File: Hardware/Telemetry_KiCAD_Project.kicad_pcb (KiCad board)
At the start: 4 copper layers, 80 x 93.3 mm, 68 parts, among them J1 TX SPI Debug, J2 RX SPI Debug, J3 50Ω SMA Connector, J4 10118192-0001LF, J5 DB37_Male_MountingHoles, U1 STM32L562VET, U2 Si4463, U3 Si4463, U4 ADL5521, U5 RSD-897.500-942.500-1612-TR, U6 LM317T, U7 USBLC6-2SC6, Y1 32MHz, Y2 32MHz, Y3 32MHz

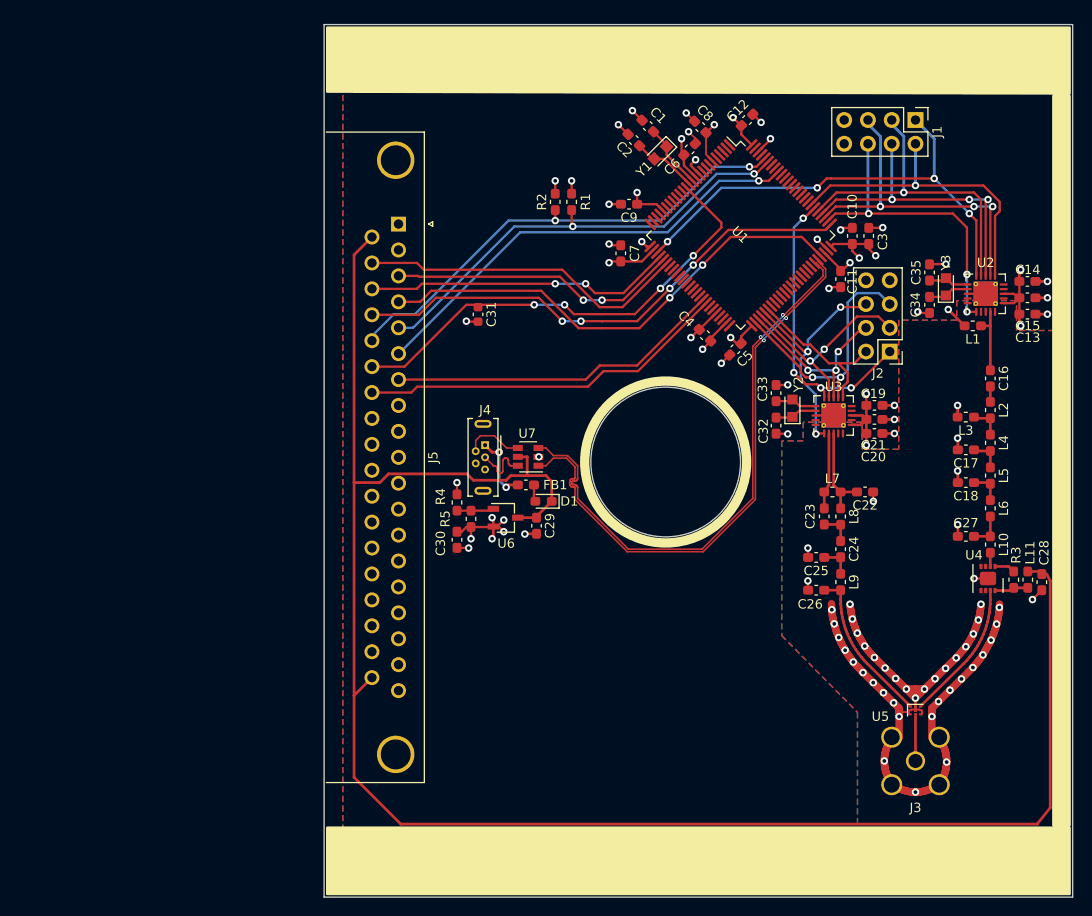
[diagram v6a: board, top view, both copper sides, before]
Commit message: Major Redesign
 - Copper ground pours on F and B.
 - Improved isolation between data lines
 - Expanded via fences around RF section.
 - GND plane isolation peninsulas for crystals.
 - Simplified I2C, SPI, and USB lines for reduced interference.
 - Added 3D models for all components.
 - Adjusted positions of RF components for improved impedance matching.
 - RF components to 0402 package from 0603 for improved impedance matching.
 - Traces for RF section have rounded corners to help improve impedance matching and reduce interference.
 - Moved silkscreen labels to outside via fence for improved legibility.
 - Improved trace thicknesses for power delivery.
 - Updated libraries to include those found in other RDT modules.
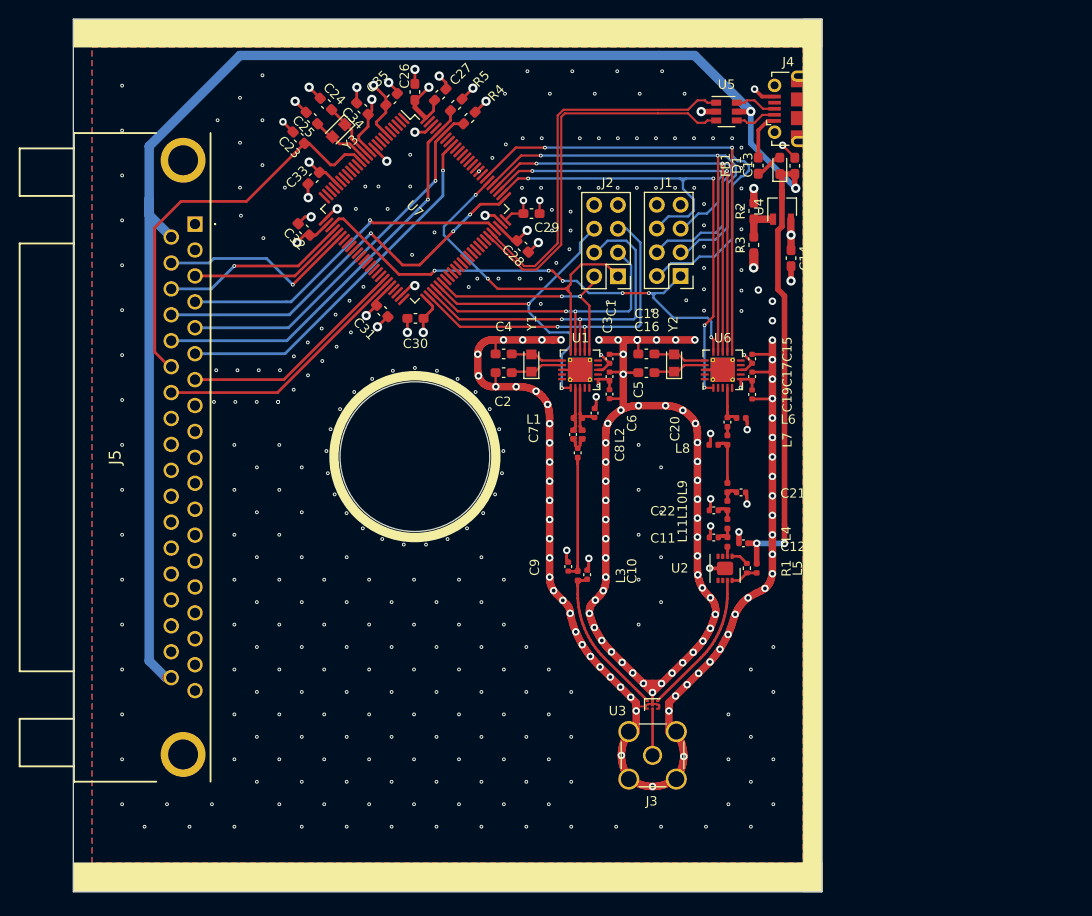
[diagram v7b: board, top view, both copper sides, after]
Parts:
- C1: value 30pF -> 100pF; footprint Capacitor_SMD:C_0603_1608Metric_Pad1.08x0.95mm_HandSolder -> Capacitor_SMD:C_0402_1005Metric
- C10, C9: value 100nF -> 4.3pF; footprint Capacitor_SMD:C_0603_1608Metric_Pad1.08x0.95mm_HandSolder -> Capacitor_SMD:C_0402_1005Metric
- C11: value 100nF -> 2.4pF; footprint Capacitor_SMD:C_0603_1608Metric_Pad1.08x0.95mm_HandSolder -> Capacitor_SMD:C_0402_1005Metric
- C12: footprint Capacitor_SMD:C_0603_1608Metric_Pad1.08x0.95mm_HandSolder -> Capacitor_SMD:C_0402_1005Metric
- C13: value 100pF -> 0.1uF
- C14: value 100pF -> 1uF
- C15, C3: value 1uF -> 100pF; footprint Capacitor_SMD:C_0603_1608Metric_Pad1.08x0.95mm_HandSolder -> Capacitor_SMD:C_0402_1005Metric
- C16: value 4.7pF -> 30pF
- C17: value 3.3pF -> 100pF; footprint Capacitor_SMD:C_0603_1608Metric_Pad1.08x0.95mm_HandSolder -> Capacitor_SMD:C_0402_1005Metric
- C18: value 3.3pF -> 30pF
- C19: value 100pF -> 1uF; footprint Capacitor_SMD:C_0603_1608Metric_Pad1.08x0.95mm_HandSolder -> Capacitor_SMD:C_0402_1005Metric
- C20: value 100pF -> 4.7pF; footprint Capacitor_SMD:C_0603_1608Metric_Pad1.08x0.95mm_HandSolder -> Capacitor_SMD:C_0402_1005Metric
- C21: value 1uF -> 3.3pF; footprint Capacitor_SMD:C_0603_1608Metric_Pad1.08x0.95mm_HandSolder -> Capacitor_SMD:C_0402_1005Metric
- C22: value 3pF -> 3.3pF; footprint Capacitor_SMD:C_0603_1608Metric_Pad1.08x0.95mm_HandSolder -> Capacitor_SMD:C_0402_1005Metric
- C23: value 1pF -> 100nF
- C24: value DC_Blocking -> 30pF
- C25: value 4.3pF -> 30pF
- C26: value 4.3pF -> 1uF
- C27: value 2.4pF -> 100nF
- C29: value 0.1uF -> 100nF
- C30: value 1uF -> 100nF
- C31: footprint Capacitor_SMD:C_0603_1608Metric -> Capacitor_SMD:C_0603_1608Metric_Pad1.08x0.95mm_HandSolder
- C32, C33, C34, C35: value 30pF -> 100nF
- C4: value 100nF -> 30pF
- C5: value 100nF -> 1uF; footprint Capacitor_SMD:C_0603_1608Metric_Pad1.08x0.95mm_HandSolder -> Capacitor_SMD:C_0402_1005Metric
- C6: value 100nF -> 3pF; footprint Capacitor_SMD:C_0603_1608Metric_Pad1.08x0.95mm_HandSolder -> Capacitor_SMD:C_0402_1005Metric
- C7: value 100nF -> 1pF; footprint Capacitor_SMD:C_0603_1608Metric_Pad1.08x0.95mm_HandSolder -> Capacitor_SMD:C_0402_1005Metric
- C8: value 100nF -> DC_Blocking; footprint Capacitor_SMD:C_0603_1608Metric_Pad1.08x0.95mm_HandSolder -> Capacitor_SMD:C_0402_1005Metric
- J3: value 50Ω SMA Connector -> Amphenol 132134 SMA Connector
- J4: footprint Connector_USB:USB_Micro-B_Wuerth_614105150721_Vertical -> Connector_USB:USB_Micro-B_Molex-105017-0001
- J5: footprint Connector_Dsub:DSUB-37_Male_Horizontal_P2.77x2.84mm_EdgePinOffset4.94mm_Housed_MountingHolesOffset7.48mm -> RDT_Custom_Footprints:L717SDC37P1ACH4F
- L1: value 100nH -> 18nH; footprint Inductor_SMD:L_0603_1608Metric_Pad1.05x0.95mm_HandSolder -> Inductor_SMD:L_0402_1005Metric
- L10: value 8.2nH -> 22nH; footprint Inductor_SMD:L_0603_1608Metric_Pad1.05x0.95mm_HandSolder -> Inductor_SMD:L_0402_1005Metric
- L11: value 3.4nH -> 11nH; footprint Inductor_SMD:L_0603_1608Metric_Pad1.05x0.95mm_HandSolder -> Inductor_SMD:L_0402_1005Metric
- L2: value 3.3nH -> 22nH; footprint Inductor_SMD:L_0603_1608Metric_Pad1.05x0.95mm_HandSolder -> Inductor_SMD:L_0402_1005Metric
- L3: value 6.2nH -> 8.2nH; footprint Inductor_SMD:L_0603_1608Metric_Pad1.05x0.95mm_HandSolder -> Inductor_SMD:L_0402_1005Metric
- L4: value 11nH -> 8.2nH; footprint Inductor_SMD:L_0603_1608Metric_Pad1.05x0.95mm_HandSolder -> Inductor_SMD:L_0402_1005Metric
- L5: value 22nH -> 3.4nH; footprint Inductor_SMD:L_0603_1608Metric_Pad1.05x0.95mm_HandSolder -> Inductor_SMD:L_0402_1005Metric
- L6: value 11nH -> 100nH; footprint Inductor_SMD:L_0603_1608Metric_Pad1.05x0.95mm_HandSolder -> Inductor_SMD:L_0402_1005Metric
- L7: value 18nH -> 3.3nH; footprint Inductor_SMD:L_0603_1608Metric_Pad1.05x0.95mm_HandSolder -> Inductor_SMD:L_0402_1005Metric
- L8: value 22nH -> 6.2nH; footprint Inductor_SMD:L_0603_1608Metric_Pad1.05x0.95mm_HandSolder -> Inductor_SMD:L_0402_1005Metric
- L9: value 8.2nH -> 11nH; footprint Inductor_SMD:L_0603_1608Metric_Pad1.05x0.95mm_HandSolder -> Inductor_SMD:L_0402_1005Metric
- R1: value 4.7k -> 1.3k; footprint Resistor_SMD:R_0603_1608Metric_Pad1.05x0.95mm_HandSolder -> Resistor_SMD:R_0402_1005Metric
- R2: value 4.7k -> 390Ω
- R3: value 1.3k -> 240Ω
- R4: value 390Ω -> 4.7k
- R5: value 240Ω -> 4.7k
- U1: value STM32L562VET -> Si4463; footprint Package_QFP:LQFP-100_14x14mm_P0.5mm -> Package_DFN_QFN:QFN-20-1EP_4x4mm_P0.5mm_EP2.6x2.6mm_ThermalVias
- U2: value Si4463 -> ADL5521; footprint Package_DFN_QFN:QFN-20-1EP_4x4mm_P0.5mm_EP2.6x2.6mm_ThermalVias -> Package_CSP:LFCSP-8-1EP_3x3mm_P0.5mm_EP1.45x1.74mm
- U3: value Si4463 -> RSD-897.500-942.500-1612-TR; footprint Package_DFN_QFN:QFN-20-1EP_4x4mm_P0.5mm_EP2.6x2.6mm_ThermalVias -> RDT_Custom_Footprints:RSD-897.500-942.500-1612-TR
- U4: value ADL5521 -> LM317T; footprint Package_CSP:LFCSP-8-1EP_3x3mm_P0.5mm_EP1.45x1.74mm -> Package_TO_SOT_SMD:TSOT-23
- U5: value RSD-897.500-942.500-1612-TR -> USBLC6-2SC6; footprint RDT_Custom_Footprints:RSD-897.500-942.500-1612-TR -> Package_TO_SOT_SMD:SOT-23-6
- U6: value LM317T -> Si4463; footprint Package_TO_SOT_SMD:TSOT-23 -> Package_DFN_QFN:QFN-20-1EP_4x4mm_P0.5mm_EP2.6x2.6mm_ThermalVias
- U7: value USBLC6-2SC6 -> STM32L562VET6Q; footprint Package_TO_SOT_SMD:SOT-23-6 -> Package_QFP:LQFP-100_14x14mm_P0.5mm
- moved C27 73.4 mm to (119.2, 59.8), turned to 45 degrees
- moved C24 72.7 mm to (107.0, 60.8), turned to 135 degrees
- moved C25 71.5 mm to (105.5, 62.3), turned to 135 degrees
- moved C23 69.2 mm to (104.1, 64.4), turned to 135 degrees
- moved C26 68.4 mm to (116.5, 59.5), turned to 90 degrees
- moved Y3 67.0 mm to (108.4, 63.6), turned to 225 degrees
- moved U5 66.3 mm to (149.8, 61.6)
- moved C28 66.1 mm to (128.0, 76.0), turned to 315 degrees
- moved C34 64.1 mm to (110.9, 61.3), turned to 135 degrees
- moved C35 60.4 mm to (114.0, 60.3), turned to 45 degrees
- moved C32 54.6 mm to (104.6, 74.2), turned to 135 degrees
- moved C33 54.5 mm to (105.7, 68.7), turned to 225 degrees
- moved J4 48.4 mm to (156.4, 61.3), turned to 90 degrees
- moved C10 46.0 mm to (134.9, 111.1)
- moved U4 45.4 mm to (155.7, 71.8), turned to 90 degrees
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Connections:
- C1 pad 1: Net-(C1-Pad1) -> GND
- C1 pad 2: GND -> +3V3
- C10 pad 1: +3V3 -> /RX_Si4463/RF_Out
- C11 pad 1: +3V3 -> GND
- C11 pad 2: GND -> /ADL_Amplifier/RF_In
- C12 pad 1: +3V3 -> GND
- C12 pad 2: GND -> +5V
- C13 pad 1: GND -> +5V
- C13 pad 2: +3V3 -> GND
- C14 pad 1: GND -> +3V3
- C14 pad 2: +3V3 -> GND
- C16 pad 2: Net-(C16-Pad2) -> GND
- C17 pad 1: Net-(C17-Pad1) -> GND
- C17 pad 2: GND -> +3V3
- C20 pad 1: GND -> Net-(C20-Pad1)
- C20 pad 2: +3V3 -> Net-(C20-Pad2)
- C21 pad 1: GND -> Net-(C21-Pad1)
- C21 pad 2: +3V3 -> GND
- C22 pad 1: GND -> Net-(C22-Pad1)
- C22 pad 2: Net-(C22-Pad2) -> GND
- C23 pad 1: Net-(C23-Pad1) -> /37 Pin DSUB/NRST
- C23 pad 2: Net-(C23-Pad2) -> GND
- C24 pad 1: Net-(C23-Pad2) -> Net-(C24-Pad1)
- C24 pad 2: Net-(C24-Pad2) -> GND
- C25 pad 1: Net-(C24-Pad2) -> Net-(C25-Pad1)
- C26 pad 1: /RX_Si4463/RF_Out -> +3V3
- C27 pad 1: GND -> +3V3
- C27 pad 2: /ADL_Amplifier/RF_In -> GND
- C28 pad 1: GND -> +3V3
- C28 pad 2: +5V -> GND
- C29 pad 1: +5V -> +3V3
- C3 pad 1: +3V3 -> GND
- C3 pad 2: GND -> +3V3
- C31 pad 1: /37 Pin DSUB/NRST -> +3V3
- C32 pad 1: Net-(C32-Pad1) -> +3V3
- C33 pad 1: Net-(C33-Pad1) -> +3V3
- C34 pad 1: Net-(C34-Pad1) -> +3V3
- C35 pad 1: Net-(C35-Pad1) -> +3V3
- C4 pad 1: +3V3 -> Net-(C4-Pad1)
- C5 pad 1: +3V3 -> GND
- C5 pad 2: GND -> +3V3
- C6 pad 1: +3V3 -> GND
- C6 pad 2: GND -> Net-(C6-Pad2)
- C7 pad 1: +3V3 -> Net-(C7-Pad1)
- C7 pad 2: GND -> Net-(C7-Pad2)
- C8 pad 1: +3V3 -> Net-(C7-Pad2)
- C8 pad 2: GND -> Net-(C8-Pad2)
- C9 pad 1: +3V3 -> Net-(C8-Pad2)
- L1 pad 1: Net-(C16-Pad1) -> Net-(C7-Pad1)
- L1 pad 2: +3V3 -> Net-(C6-Pad2)
- L10 pad 1: /ADL_Amplifier/RF_In -> Net-(C21-Pad1)
- L10 pad 2: Net-(L10-Pad2) -> Net-(C22-Pad1)
- L11 pad 1: Net-(L11-Pad1) -> Net-(C22-Pad1)
- L11 pad 2: +5V -> /ADL_Amplifier/RF_In
- L2 pad 1: Net-(C16-Pad2) -> Net-(C6-Pad2)
- L2 pad 2: Net-(L2-Pad2) -> Net-(C7-Pad2)
- L3 pad 1: Net-(L2-Pad2) -> Net-(C8-Pad2)
- L3 pad 2: GND -> /RX_Si4463/RF_Out
- L4 pad 1: Net-(L2-Pad2) -> /ADL_Amplifier/RF_In
- L4 pad 2: Net-(C17-Pad1) -> Net-(L4-Pad2)
- L5 pad 1: Net-(C17-Pad1) -> Net-(L5-Pad1)
- L5 pad 2: Net-(C18-Pad1) -> +5V
- L6 pad 1: Net-(C18-Pad1) -> Net-(C20-Pad1)
- L6 pad 2: /ADL_Amplifier/RF_In -> +3V3
- L7 pad 1: Net-(C23-Pad1) -> Net-(C20-Pad2)
- L7 pad 2: Net-(C22-Pad2) -> Net-(L7-Pad2)
- L8 pad 1: Net-(C22-Pad2) -> Net-(L7-Pad2)
- L8 pad 2: Net-(C23-Pad2) -> GND
- L9 pad 1: Net-(C24-Pad2) -> Net-(L7-Pad2)
- L9 pad 2: /RX_Si4463/RF_Out -> Net-(C21-Pad1)
- R1 pad 1: /37 Pin DSUB/Alert_scl -> Net-(L5-Pad1)
- R1 pad 2: +3V3 -> Net-(R1-Pad2)
- R2 pad 1: /37 Pin DSUB/Alert_sda -> Net-(R2-Pad1)
- R2 pad 2: +3V3 -> GND
- R3 pad 1: Net-(L11-Pad1) -> +3V3
- R3 pad 2: Net-(R3-Pad2) -> Net-(R2-Pad1)
- R4 pad 1: Net-(R4-Pad1) -> /37 Pin DSUB/Alert_scl
- R4 pad 2: GND -> +3V3
- R5 pad 1: +3V3 -> /37 Pin DSUB/Alert_sda
- R5 pad 2: Net-(R4-Pad1) -> +3V3
- U1 pad 1: Net-(U1-Pad1) -> /RX_RST
- U1 pad 10: GND -> Net-(U1-Pad10)
- U1 pad 11: +3V3 -> /~RX_IRQ
- U1 pad 12: Net-(C1-Pad1) -> /RX_SCL
- U1 pad 13: Net-(C2-Pad1) -> /RX_SDO
- U1 pad 14: /37 Pin DSUB/NRST -> /RX_SDI
- U1 pad 15: Net-(U1-Pad15) -> /~RX_SEL
- U1 pad 16: Net-(U1-Pad16) -> Net-(C4-Pad1)
- U1 pad 17: Net-(U1-Pad17) -> Net-(C2-Pad1)
- U1 pad 18: Net-(U1-Pad18) -> GND
- U1 pad 2: Net-(U1-Pad2) -> Net-(C7-Pad1)
- U1 pad 21: +3V3 -> GND
- U1 pad 3: Net-(U1-Pad3) -> Net-(C6-Pad2)
- U1 pad 8: Net-(U1-Pad8) -> +3V3
- U2 pad 1: /TX_RST -> Net-(R1-Pad2)
- U2 pad 2: Net-(U2-Pad2) -> Net-(L4-Pad2)
- U2 pad 3: Net-(U2-Pad3) -> (no net)
- U2 pad 4: Net-(C16-Pad1) -> (no net)
- U2 pad 5: Net-(U2-Pad5) -> (no net)
- U2 pad 6: +3V3 -> (no net)
- U2 pad 7: Net-(U2-Pad7) -> /ADL_Amplifier/RF_Out
- U2 pad 8: +3V3 -> Net-(L5-Pad1)
- U2 pad 9: Net-(U2-Pad9) -> GND
- U3 pad 1: /RX_RST -> /RX_Si4463/RF_Out
- U3 pad 2: Net-(C23-Pad1) -> GND
- U3 pad 3: Net-(C22-Pad2) -> /ADL_Amplifier/RF_Out
- U3 pad 4: Net-(U3-Pad4) -> GND
- U3 pad 5: Net-(U3-Pad5) -> GND
- U3 pad 6: +3V3 -> /RSD_Duplexer/Antenna
- U3 pad 7: Net-(U3-Pad7) -> GND
- U3 pad 8: +3V3 -> GND
- U4 pad 1: Net-(R3-Pad2) -> Net-(R2-Pad1)
- U4 pad 2: Net-(L10-Pad2) -> +3V3
- U4 pad 3: (no net) -> +5V
- U5 pad 1: /RX_Si4463/RF_Out -> /USB Connector and ESD/D+
- U5 pad 3: /ADL_Amplifier/RF_Out -> /USB Connector and ESD/D-
- U5 pad 4: GND -> /USB Connector and ESD/USB_CONN_D-
- U5 pad 5: GND -> +5V
- U5 pad 6: /RSD_Duplexer/Antenna -> /USB Connector and ESD/USB_CONN_D+
- U6 pad 1: Net-(R4-Pad1) -> /TX_RST
- U6 pad 2: +3V3 -> Net-(U6-Pad2)
- U6 pad 3: +5V -> Net-(U6-Pad3)
- U7 pad 1: /USB Connector and ESD/D+ -> Net-(U7-Pad1)
- U7 pad 2: GND -> Net-(U7-Pad2)
- U7 pad 3: /USB Connector and ESD/D- -> Net-(U7-Pad3)
- U7 pad 4: /USB Connector and ESD/USB_CONN_D- -> Net-(U7-Pad4)
- U7 pad 5: +5V -> Net-(U7-Pad5)
- U7 pad 6: /USB Connector and ESD/USB_CONN_D+ -> +3V3
- Y1 pad 1: Net-(C1-Pad1) -> Net-(C2-Pad1)
- Y1 pad 2: Net-(C2-Pad1) -> Net-(C4-Pad1)
- Y2 pad 1: Net-(C32-Pad1) -> Net-(C16-Pad1)
- Y2 pad 2: Net-(C33-Pad1) -> Net-(C18-Pad1)
- Y3 pad 1: Net-(C34-Pad1) -> Net-(C24-Pad1)
- Y3 pad 2: Net-(C35-Pad1) -> Net-(C25-Pad1)
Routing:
- net GND: track 146.9 -> 308.4 mm, vias 79 -> 404
- net /~TX_IRQ: track 34.3 -> 71.0 mm, vias 1 -> 2
- net /TX_SDO: track 32.7 -> 61.5 mm, vias 3 -> 2
- net /TX_SDI: track 35.0 -> 61.8 mm, vias 1 -> 2
- net /TX_RST: track 33.3 -> 56.3 mm, vias 3 -> 4
- net /USB Connector and ESD/D+: track 62.1 -> 40.8 mm, vias 2 -> 0
- net /USB Connector and ESD/D-: track 61.5 -> 41.1 mm, vias 2 -> 0
- net /RX_SDO: track 19.8 -> 39.0 mm, vias 3 -> 2
- net /TX_SCL: track 35.8 -> 53.6 mm, vias 3 -> 2
- net /MCU_L562VE/DEBUG_SWDIO: track 52.2 -> 36.3 mm, vias 2 -> 1
- net Net-(C8-Pad2): track 0.00 -> 14.6 mm
- net /MCU_L562VE/SPI1_MISO: track 31.2 -> 17.1 mm, vias 2 -> 0
- net /MCU_L562VE/SPI1_MOSI: track 35.4 -> 21.6 mm, vias 0 -> 1
- net /MCU_L562VE/SPI1_SCK: track 33.3 -> 20.0 mm, vias 2 -> 1
- net /MCU_L562VE/ABORT_2: track 39.7 -> 27.9 mm
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- added copper zone on 3.3V.Cu, net +3V3
- added copper zone on GND.Cu, net GND
- removed copper zone on Pwr.Cu, net +3V3
- removed copper zone on Gnd.Cu, net GND
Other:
- board size 80 x 93.3 mm -> 80 x 93.2 mm
- net class 900MHZ_RF_50OHM removed
- net class DIFF_90_USB removed
- net class Default: clearance 0.05 -> 0.5; trace_width 0.25 -> 0.2
- net class Mostly Safe Minimums added: clearance 0.127, trace_width 0.127, via_dia 0.45, via_drill 0.3
- net class Trace Minimums added: clearance 0.2, trace_width 0.15, via_dia 0.8, via_drill 0.4
- net class Trace to Trace Abs. Minimums added: clearance 0.09, trace_width 0.09, via_dia 0.8, via_drill 0.4
- net class USB_Diff added: clearance 0.1524, trace_width 0.228854, via_dia 0.8, via_drill 0.4
- net class Via Different Net Minimums added: clearance 0.5, trace_width 0.15, via_dia 0.4, via_drill 0.2
- net class Via Same Net Minimums added: clearance 0.254, trace_width 0.2, via_dia 0.4, via_drill 0.2
- rule trace_clearance: 0.05 -> 0.5

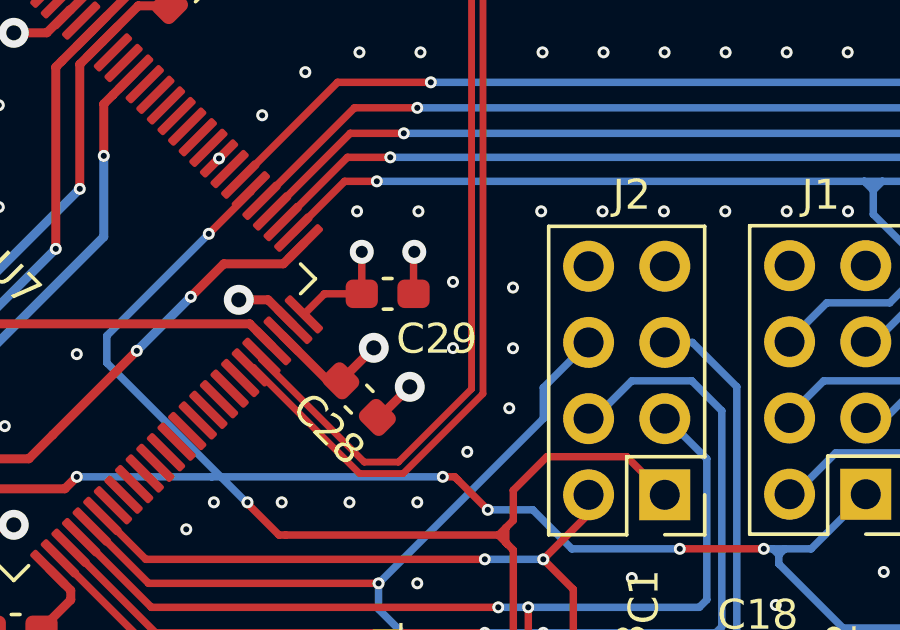
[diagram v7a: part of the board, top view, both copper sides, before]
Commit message: Connected some unconnected GND stitching vias
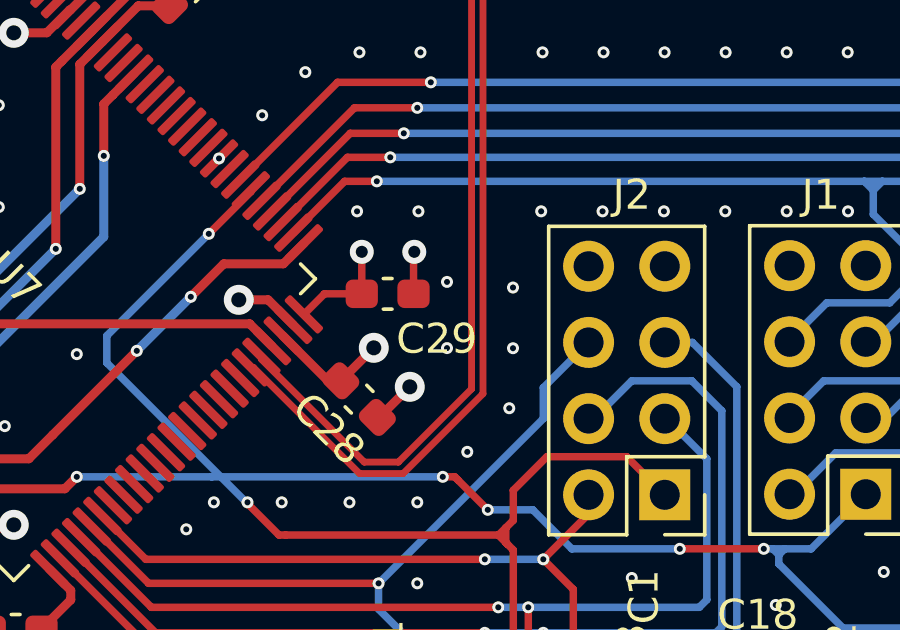
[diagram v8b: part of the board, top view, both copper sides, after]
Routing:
- net GND: vias 404 -> 413
- net (no net): vias 9 -> 0
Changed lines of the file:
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@@
   (target plus (at 80 144.975) (size 5) (width 0.05) (layer Edge.Cuts))
   (gr_circle (center 116.5 98.475) (end 124.5 98.475) (layer Edge.Cuts) (width 0.05))
-  (via (at 140.525 59.690002) (size 0.4) (drill 0.2) (layers F.Cu B.Cu) (net 0))
-  (via (at 133.325 57.290001) (size 0.4) (drill 0.2) (layers F.Cu B.Cu) (net 0))
-  (via (at 126.125 59.690001) (size 0.4) (drill 0.2) (layers F.Cu B.Cu) (net 0))
-  (via (at 142.925 57.290001) (size 0.4) (drill 0.2) (layers F.Cu B.Cu) (net 0))
-  (via (at 145.325 59.690001) (size 0.4) (drill 0.2) (layers F.Cu B.Cu) (net 0))
-  (via (at 130.925 59.690002) (size 0.4) (drill 0.2) (layers F.Cu B.Cu) (net 0))
-  (via (at 128.525 57.290001) (size 0.4) (drill 0.2) (layers F.Cu B.Cu) (net 0))
-  (via (at 138.125 57.290001) (size 0.4) (drill 0.2) (layers F.Cu B.Cu) (net 0))
-  (via (at 135.725 59.690001) (size 0.4) (drill 0.2) (layers F.Cu B.Cu) (net 0))
+  (via (at 140.525 59.690002) (size 0.4) (drill 0.2) (layers F.Cu B.Cu) (net 1))
+  (via (at 133.325 57.290001) (size 0.4) (drill 0.2) (layers F.Cu B.Cu) (net 1))
+  (via (at 126.125 59.690001) (size 0.4) (drill 0.2) (layers F.Cu B.Cu) (net 1))
+  (via (at 142.925 57.290001) (size 0.4) (drill 0.2) (layers F.Cu B.Cu) (net 1))
+  (via (at 145.325 59.690001) (size 0.4) (drill 0.2) (layers F.Cu B.Cu) (net 1))
+  (via (at 130.925 59.690002) (size 0.4) (drill 0.2) (layers F.Cu B.Cu) (net 1))
+  (via (at 128.525 57.290001) (size 0.4) (drill 0.2) (layers F.Cu B.Cu) (net 1))
+  (via (at 138.125 57.290001) (size 0.4) (drill 0.2) (layers F.Cu B.Cu) (net 1))
+  (via (at 135.725 59.690001) (size 0.4) (drill 0.2) (layers F.Cu B.Cu) (net 1))
   (via (at 97.909999 72.725) (size 0.4) (drill 0.2) (layers F.Cu B.Cu) (net 1))
   (via (at 100.31 75.125) (size 0.4) (drill 0.2) (layers F.Cu B.Cu) (net 1))
@@
   (via (at 133.140627 74.312002) (size 0.4) (drill 0.2) (layers F.Cu B.Cu) (net 1))
   (via (at 133.140627 72.289828) (size 0.4) (drill 0.2) (layers F.Cu B.Cu) (net 1))
-  (via (at 131.140627 72.102818) (size 0.4) (drill 0.2) (layers F.Cu B.Cu) (net 1))
-  (via (at 131.140627 74.308782) (size 0.4) (drill 0.2) (layers F.Cu B.Cu) (net 1))
+  (via (at 130.940627 72.102818) (size 0.4) (drill 0.2) (layers F.Cu B.Cu) (net 1))
+  (via (at 130.940627 74.308782) (size 0.4) (drill 0.2) (layers F.Cu B.Cu) (net 1))
   (via (at 129.95005 79.45) (size 0.4) (drill 0.2) (layers F.Cu B.Cu) (net 1))
   (via (at 127.690101 79.45) (size 0.4) (drill 0.2) (layers F.Cu B.Cu) (net 1))
